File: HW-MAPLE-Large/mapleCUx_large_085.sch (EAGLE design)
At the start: 56 parts, among them IC1 DS2482, IC2 LAN-USR-ES1, Q1 BSS84, X4 1751248, X7 1751264

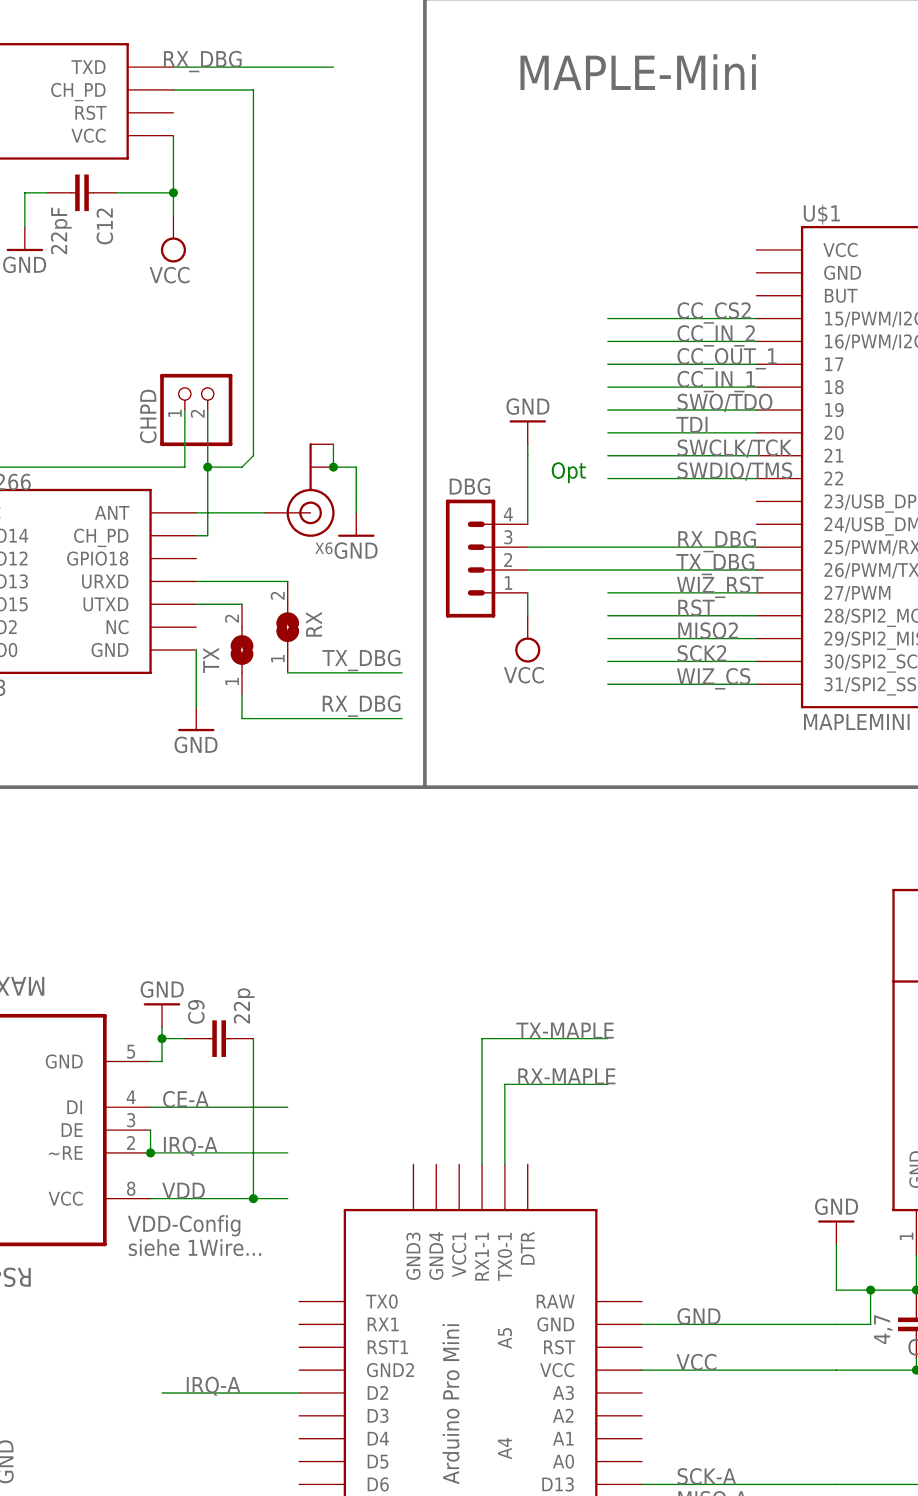
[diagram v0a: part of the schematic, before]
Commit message: Small Fixes + other RX+TX Pins at Arduino
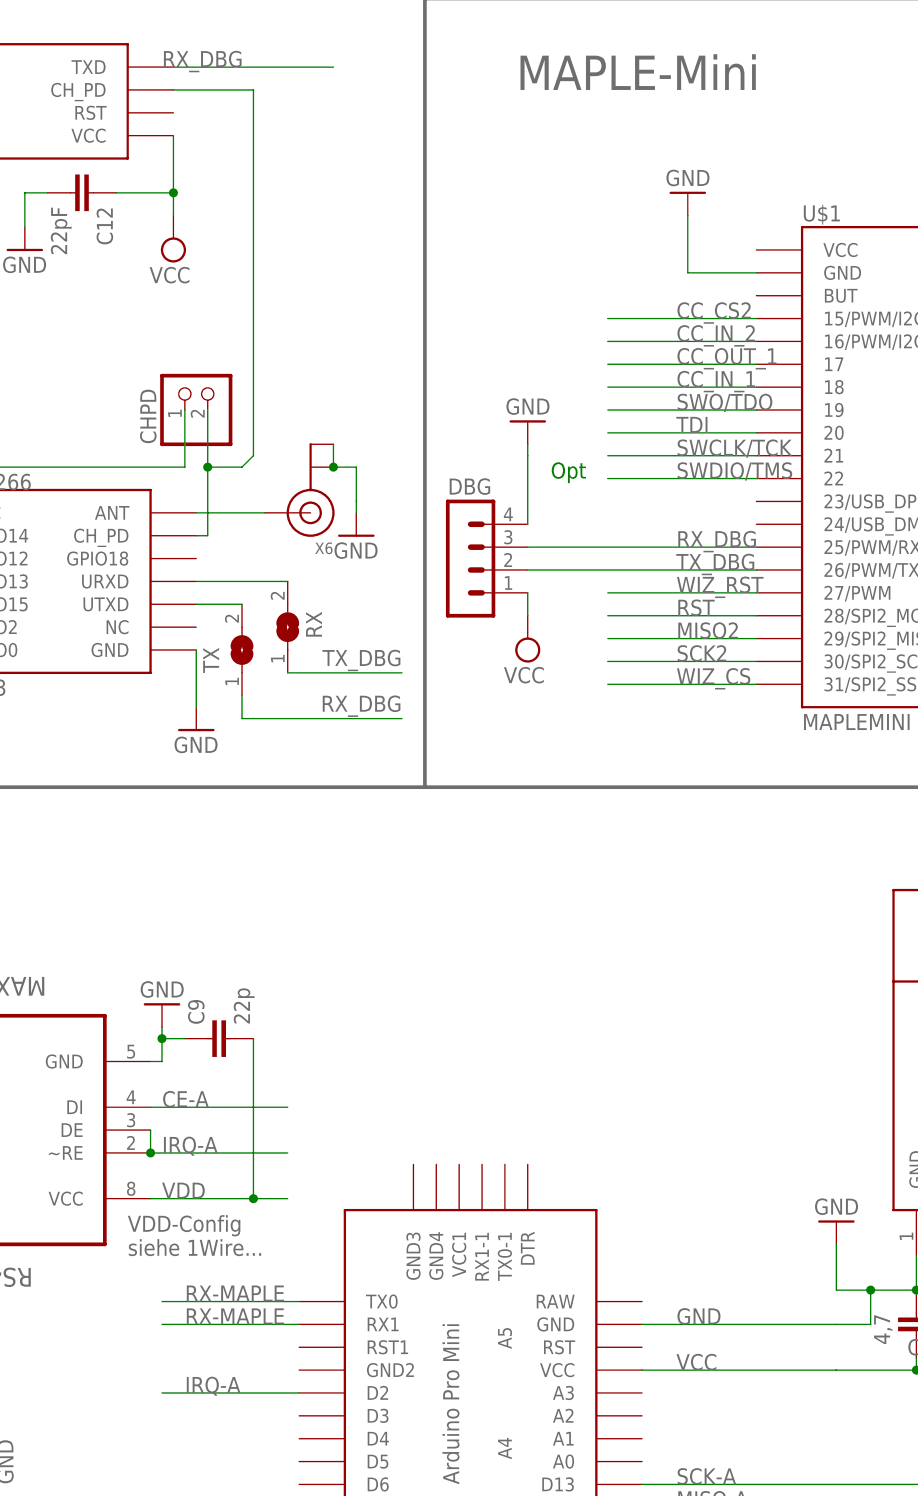
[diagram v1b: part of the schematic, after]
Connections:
- net GND: now also U$1.GND
- net RX-MAPLE: now also U$2.RX1, U$2.TX0; no longer U$2.TX0-1
- net TX-MAPLE: no longer U$2.RX1-1
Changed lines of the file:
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@@
 <setting verticaltext="up"/>
 </settings>
-<grid distance="0.1" unitdist="inch" unit="inch" style="lines" multiple="1" display="no" altdistance="0.01" altunitdist="inch" altunit="inch"/>
+<grid distance="50" unitdist="mil" unit="mil" style="lines" multiple="1" display="no" altdistance="0.01" altunitdist="inch" altunit="inch"/>
 <layers>
 <layer number="1" name="Top" color="4" fill="1" visible="no" active="no"/>
@@
 <part name="C12" library="rcl" deviceset="C-EU" device="C0805" value="22pF"/>
 <part name="GND17" library="supply1" deviceset="GND" device=""/>
+<part name="GND6" library="supply1" deviceset="GND" device=""/>
 </parts>
 <sheets>
@@
 <instance part="C12" gate="G$1" x="49.53" y="165.1" rot="R270"/>
 <instance part="GND17" gate="1" x="41.91" y="158.75"/>
+<instance part="GND6" gate="1" x="115.57" y="165.1" rot="R180"/>
 </instances>
 <busses>
@@
 <wire x1="41.91" y1="165.1" x2="41.91" y2="161.29" width="0.1524" layer="91"/>
 </segment>
+<segment>
+<pinref part="U$1" gate="G$1" pin="GND"/>
+<pinref part="GND6" gate="1" pin="GND"/>
+<wire x1="123.19" y1="156.21" x2="115.57" y2="156.21" width="0.1524" layer="91"/>
+<wire x1="115.57" y1="156.21" x2="115.57" y2="162.56" width="0.1524" layer="91"/>
+</segment>
 </net>
 <net name="+5V" class="1">
@@
 </segment>
 <segment>
-<pinref part="U$2" gate="G$1" pin="TX0-1"/>
-<wire x1="95.25" y1="57.15" x2="95.25" y2="66.04" width="0.1524" layer="91"/>
-<wire x1="95.25" y1="66.04" x2="106.68" y2="66.04" width="0.1524" layer="91"/>
-<label x="96.52" y="66.04" size="1.778" layer="95"/>
+<pinref part="U$2" gate="G$1" pin="TX0"/>
+<wire x1="72.39" y1="41.91" x2="57.15" y2="41.91" width="0.1524" layer="91"/>
+<label x="59.69" y="41.91" size="1.778" layer="95"/>
+</segment>
+<segment>
+<pinref part="U$2" gate="G$1" pin="RX1"/>
+<wire x1="72.39" y1="39.37" x2="57.15" y2="39.37" width="0.1524" layer="91"/>
+<label x="59.69" y="39.37" size="1.778" layer="95"/>
 </segment>
 </net>
@@
 <label x="203.2" y="135.89" size="1.778" layer="95"/>
 </segment>
-<segment>
-<pinref part="U$2" gate="G$1" pin="RX1-1"/>
-<wire x1="92.71" y1="57.15" x2="92.71" y2="71.12" width="0.1524" layer="91"/>
-<wire x1="92.71" y1="71.12" x2="106.68" y2="71.12" width="0.1524" layer="91"/>
-<label x="96.52" y="71.12" size="1.778" layer="95"/>
-</segment>
-</net>
+</net>
